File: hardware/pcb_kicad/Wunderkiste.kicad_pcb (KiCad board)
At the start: 2 copper layers, 173.2 x 225 mm, 60 parts, among them J1 Conn_01x10, J10 Headphones, J11 Spkr_R, J2 SD_Card_Det, J3 Powerbank, J4 STM32F4_Discovery, J5 USB_B, J6 Conn_01x16, J7 Conn_01x16, J8 Spkr_L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

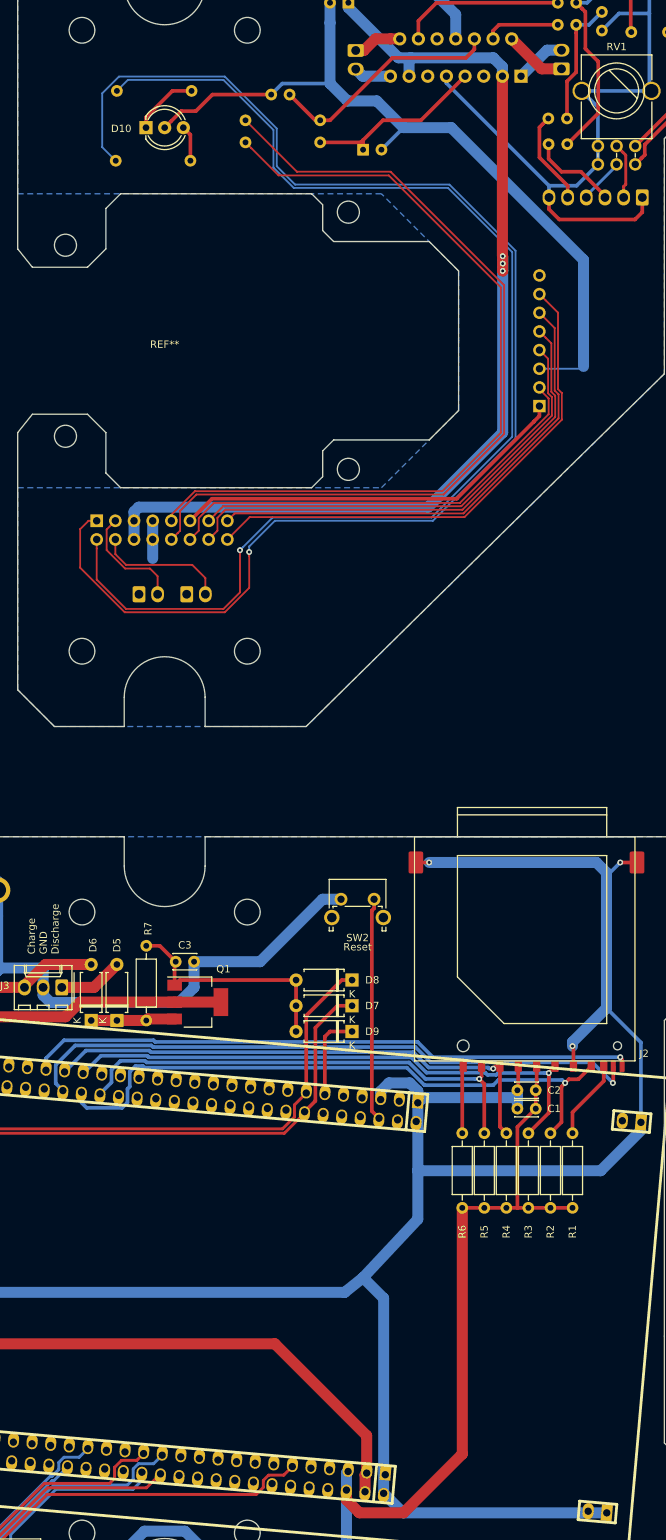
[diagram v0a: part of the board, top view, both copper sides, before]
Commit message: Fixed DRC errors in the pcb file
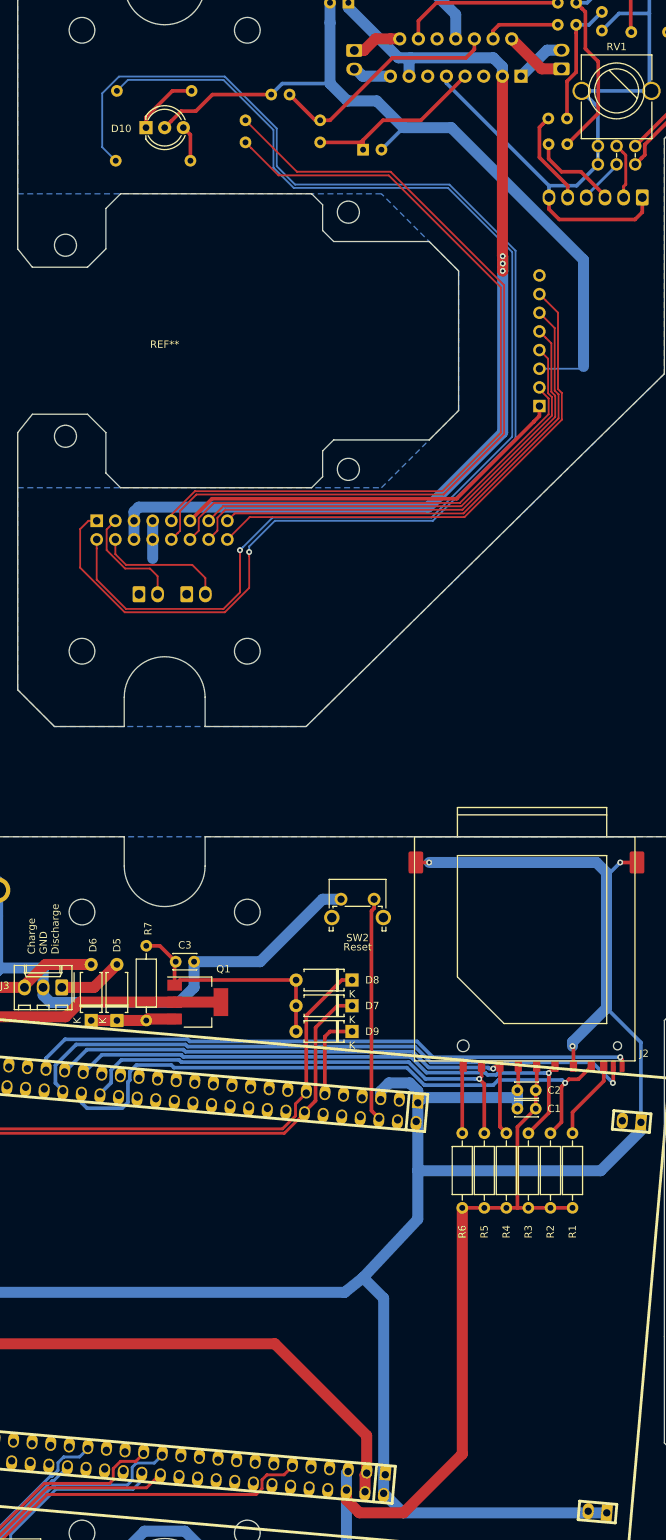
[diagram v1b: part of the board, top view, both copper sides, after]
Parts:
- moved J11 0.19 mm to (225.8, 60.5)
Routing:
- net /RFID_CS: track 47.5 -> 47.7 mm, vias 1 -> 0

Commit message: Improved drill template on the Dwgs.User layer
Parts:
- renumbered REF** to #Ref**
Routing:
- net /AMP_STBY_T: track 113.0 -> 117.8 mm
- net /AMP_MUTE_T: track 117.6 -> 122.3 mm
- net /TOP_LED_R_T: track 169.0 -> 170.1 mm
- net +5V: track 328.8 -> 329.7 mm
- net /TOP_LED_G_T: track 188.3 -> 188.9 mm
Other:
- outline, holes or cut-outs redrawn
- board text added: "1. Print at 100% scale 2. Check print dimensions with the scale check ruler 3. Apply from the inside to the top surface of the case, align with mounting holes and mark drill positions with a punch tool or nail."
- board text added: "Drill Template"
- board text added: "v0.2"
- board text removed: "v0.1"
